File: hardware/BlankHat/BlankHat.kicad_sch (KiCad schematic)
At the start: 9 parts, among them J1 Conn_01x08_Socket, J2 Conn_01x08_Socket, J3 Conn_01x08_Socket, Q1 PZT2222A, U1 74HC688, U2 74HC245, U3 74HC245

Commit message: designing new main board
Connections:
- net at J2.1 (Pin_1): now also U2.9 (A7); no longer U2.2 (A0)
- net at J2.2 (Pin_2): now also U2.8 (A6); no longer U2.3 (A1)
- net at J2.3 (Pin_3): now also U2.7 (A5); no longer U2.4 (A2)
- net at J2.4 (Pin_4): now also U2.6 (A4); no longer U2.5 (A3)
- net at J2.5 (Pin_5): now also U2.5 (A3); no longer U2.6 (A4)
- net at J2.6 (Pin_6): now also U2.4 (A2); no longer U2.7 (A5)
- net at J2.7 (Pin_7): now also U2.3 (A1); no longer U2.8 (A6)
- net at J2.8 (Pin_8): now also U2.2 (A0); no longer U2.9 (A7)
- net at U3.2 (A0): now also J3.8 (Pin_8); no longer J3.1 (Pin_1)
- net at U3.3 (A1): now also J3.7 (Pin_7); no longer J3.2 (Pin_2)
- net at U3.4 (A2): now also J3.6 (Pin_6); no longer J3.3 (Pin_3)
- net at U3.5 (A3): now also J3.5 (Pin_5); no longer J3.4 (Pin_4)
- net at U3.6 (A4): now also J3.4 (Pin_4); no longer J3.5 (Pin_5)
- net at U3.7 (A5): now also J3.3 (Pin_3); no longer J3.6 (Pin_6)
- net at U3.8 (A6): now also J3.2 (Pin_2); no longer J3.7 (Pin_7)
- net at U3.9 (A7): now also J3.1 (Pin_1); no longer J3.8 (Pin_8)
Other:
- moved on the sheet: J2, J3
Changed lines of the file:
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@@
 	(symbol
 		(lib_id "Connector:Conn_01x08_Socket")
-		(at 187.96 69.85 0)
-		(mirror y)
+		(at 187.96 72.39 180)
 		(unit 1)
 		(exclude_from_sim no)
@@
 		(dnp no)
 		(property "Reference" "J2"
-			(at 190.5 56.896 0)
+			(at 191.008 56.896 0)
 			(effects
 				(font
@@
 		)
 		(property "Value" "Conn_01x08_Socket"
-			(at 188.595 82.55 0)
+			(at 188.595 59.69 0)
 			(effects
 				(font
@@
 		)
 		(property "Footprint" "Connector_PinSocket_2.54mm:PinSocket_1x08_P2.54mm_Vertical"
-			(at 187.96 69.85 0)
+			(at 187.96 72.39 0)
 			(effects
 				(font
@@
 		)
 		(property "Datasheet" "~"
-			(at 187.96 69.85 0)
+			(at 187.96 72.39 0)
 			(effects
 				(font
@@
 		)
 		(property "Description" "Generic connector, single row, 01x08, script generated"
-			(at 187.96 69.85 0)
+			(at 187.96 72.39 0)
 			(effects
 				(font
@@
 	(symbol
 		(lib_id "Connector:Conn_01x08_Socket")
-		(at 231.14 69.85 0)
-		(mirror y)
+		(at 231.14 72.39 180)
 		(unit 1)
 		(exclude_from_sim no)
@@
 		(dnp no)
 		(property "Reference" "J3"
-			(at 233.68 56.896 0)
+			(at 233.68 55.88 0)
 			(effects
 				(font
@@
 		)
 		(property "Value" "Conn_01x08_Socket"
-			(at 231.775 82.55 0)
+			(at 231.775 59.69 0)
 			(effects
 				(font
@@
 		)
 		(property "Footprint" "Connector_PinSocket_2.54mm:PinSocket_1x08_P2.54mm_Vertical"
-			(at 231.14 69.85 0)
+			(at 231.14 72.39 0)
 			(effects
 				(font
@@
 		)
 		(property "Datasheet" "~"
-			(at 231.14 69.85 0)
+			(at 231.14 72.39 0)
 			(effects
 				(font
@@
 		)
 		(property "Description" "Generic connector, single row, 01x08, script generated"
-			(at 231.14 69.85 0)
-			(effects
-				(font
+			(at 231.14 72.39 0)
+			(effects
+				(font

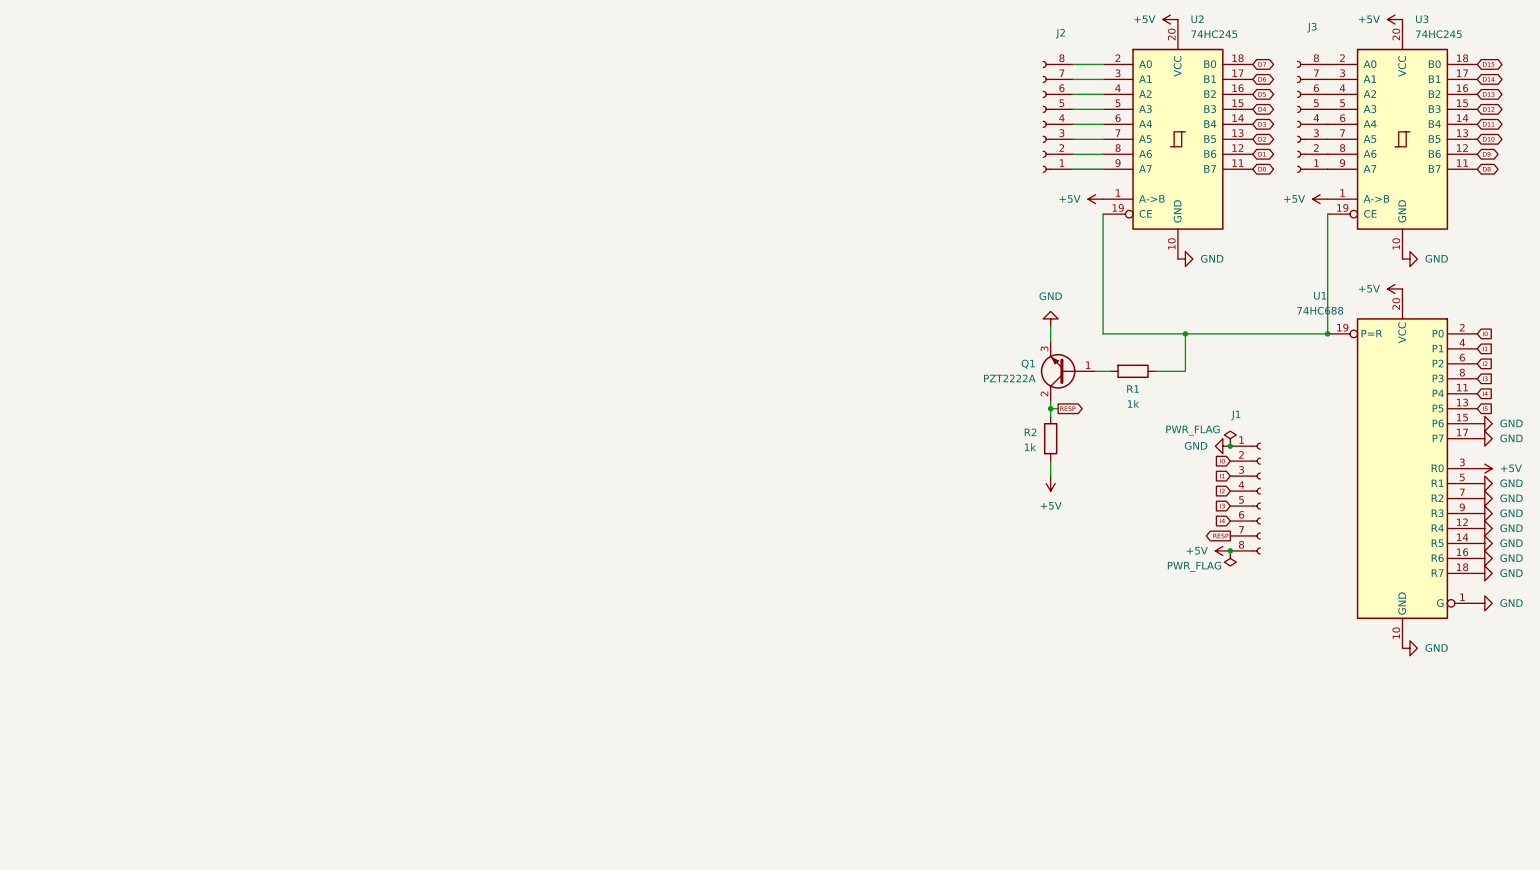
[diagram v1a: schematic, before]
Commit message: made the blank hat with correct footprint
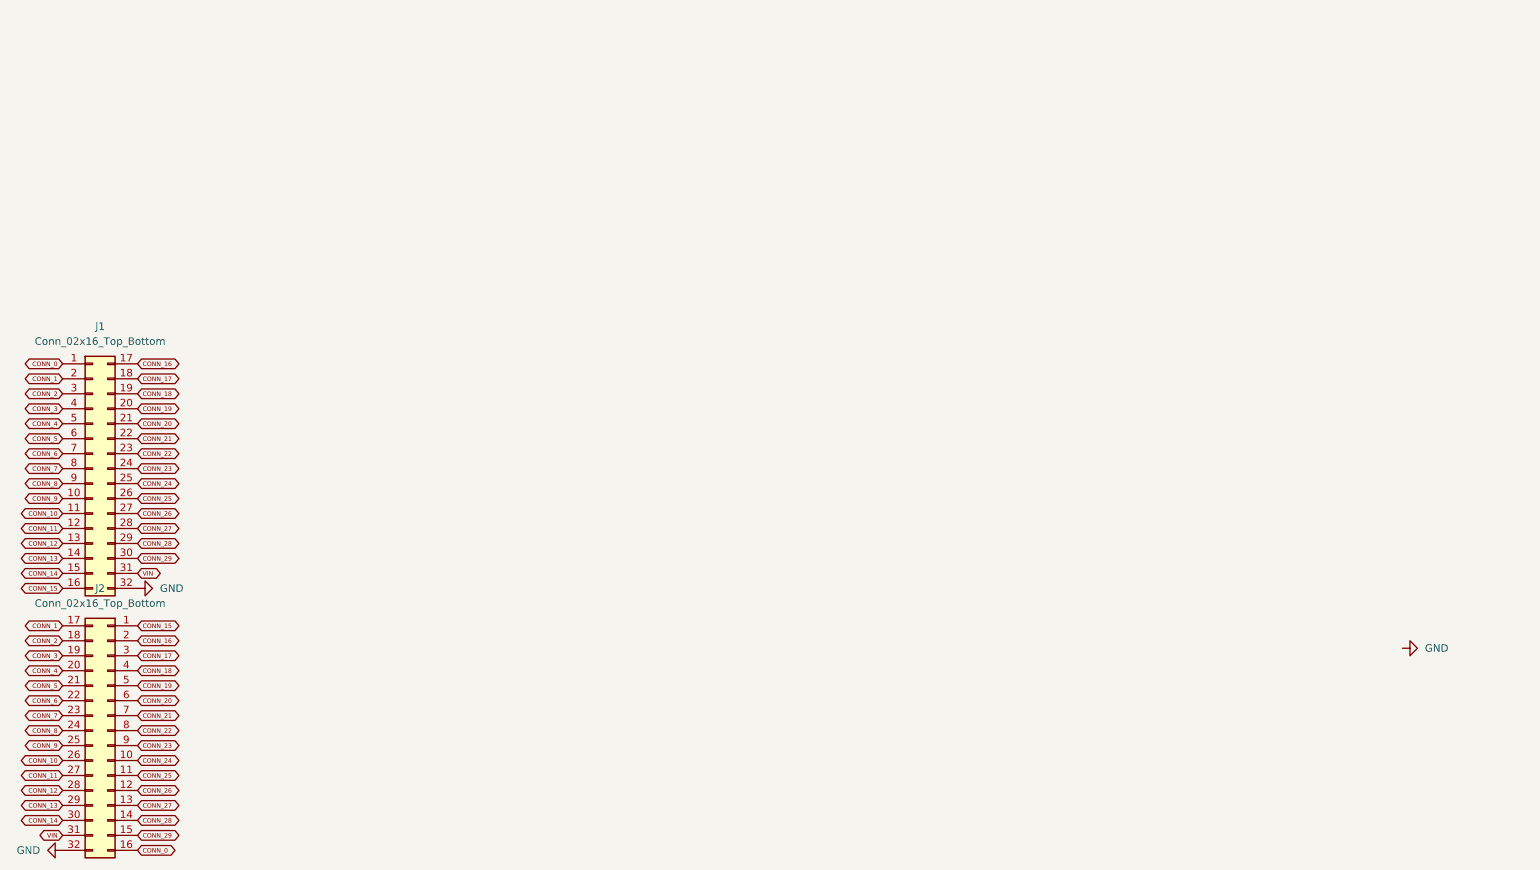
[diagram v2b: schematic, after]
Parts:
- removed J1, J2, J3: Conn_01x08_Socket, Connector_PinSocket_2.54mm:PinSocket_1x08_P2.54mm_Vertical, symbol Connector:Conn_01x08_Socket
- removed Q1: PZT2222A, Package_TO_SOT_SMD:SOT-223-3_TabPin2, symbol Transistor_BJT:PZT2222A
- removed R1, R2: 1k, Resistor_SMD:R_0201_0603Metric, symbol Device:R
- removed U1: 74HC688, Package_SO:TSSOP-20_4.4x6.5mm_P0.65mm, symbol 74xx:74HC688
- removed U2, U3: 74HC245, Package_SO:TSSOP-20_4.4x6.5mm_P0.65mm, symbol 74xx:74HC245
- added J1: Conn_02x16_Top_Bottom, MolexFSB:FSB5 Series 0.40 mm Pitch Floating SlimStack Board-to-Board Receptacles, symbol Connector_Generic:Conn_02x16_Top_Bottom
- added J2: Conn_02x16_Top_Bottom, MolexFSB:FSB5 Series 0.40 mm Pitch Floating SlimStack Board-to-Board Plugs, symbol Connector_Generic:Conn_02x16_Top_Bottom
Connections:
- net GND: now also J1.32 (Pin_32), J2.32 (Pin_32)
- new net CONN_0: J1.1 (Pin_1), J2.16 (Pin_16)
- new net CONN_1: J1.2 (Pin_2), J2.17 (Pin_17)
- new net CONN_10: J1.11 (Pin_11), J2.26 (Pin_26)
- new net CONN_11: J1.12 (Pin_12), J2.27 (Pin_27)
- new net CONN_12: J1.13 (Pin_13), J2.28 (Pin_28)
- new net CONN_13: J1.14 (Pin_14), J2.29 (Pin_29)
- new net CONN_14: J1.15 (Pin_15), J2.30 (Pin_30)
- new net CONN_15: J1.16 (Pin_16), J2.1 (Pin_1)
- new net CONN_16: J1.17 (Pin_17), J2.2 (Pin_2)
- new net CONN_17: J1.18 (Pin_18), J2.3 (Pin_3)
- new net CONN_18: J1.19 (Pin_19), J2.4 (Pin_4)
- new net CONN_19: J1.20 (Pin_20), J2.5 (Pin_5)
- new net CONN_2: J1.3 (Pin_3), J2.18 (Pin_18)
- new net CONN_20: J1.21 (Pin_21), J2.6 (Pin_6)
- new net CONN_21: J1.22 (Pin_22), J2.7 (Pin_7)
- new net CONN_22: J1.23 (Pin_23), J2.8 (Pin_8)
- new net CONN_23: J1.24 (Pin_24), J2.9 (Pin_9)
- new net CONN_24: J1.25 (Pin_25), J2.10 (Pin_10)
- new net CONN_25: J1.26 (Pin_26), J2.11 (Pin_11)
- new net CONN_26: J1.27 (Pin_27), J2.12 (Pin_12)
- new net CONN_27: J1.28 (Pin_28), J2.13 (Pin_13)
- new net CONN_28: J1.29 (Pin_29), J2.14 (Pin_14)
- new net CONN_29: J1.30 (Pin_30), J2.15 (Pin_15)
- new net CONN_3: J1.4 (Pin_4), J2.19 (Pin_19)
- new net CONN_4: J1.5 (Pin_5), J2.20 (Pin_20)
- new net CONN_5: J1.6 (Pin_6), J2.21 (Pin_21)
- new net CONN_6: J1.7 (Pin_7), J2.22 (Pin_22)
- new net CONN_7: J1.8 (Pin_8), J2.23 (Pin_23)
- new net CONN_8: J1.9 (Pin_9), J2.24 (Pin_24)
- new net CONN_9: J1.10 (Pin_10), J2.25 (Pin_25)
- new net VIN: J1.31 (Pin_31), J2.31 (Pin_31)
